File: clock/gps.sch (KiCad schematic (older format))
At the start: 12 parts, among them P301 MCRF, Q301 BSS138, U301 Adafruit746, U302 MIC5225, U303 PA6H

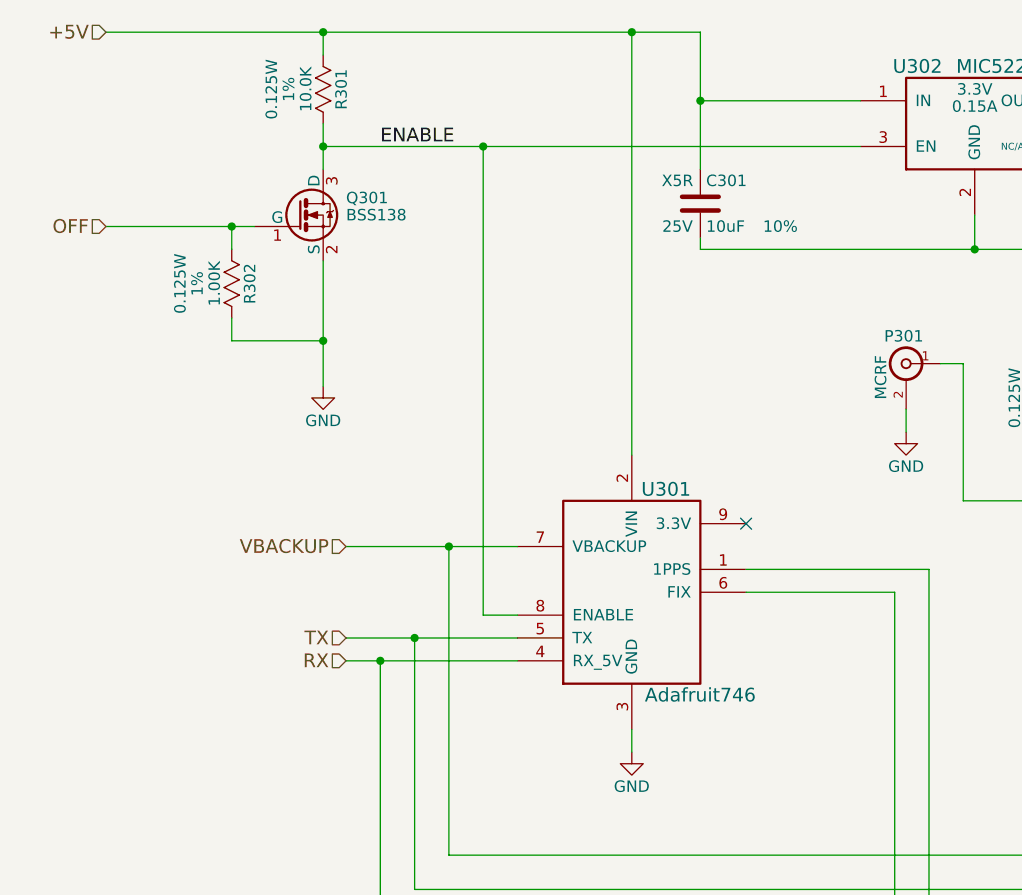
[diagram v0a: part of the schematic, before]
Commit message: Start next revision of the main board. Power sequencing and control changes.
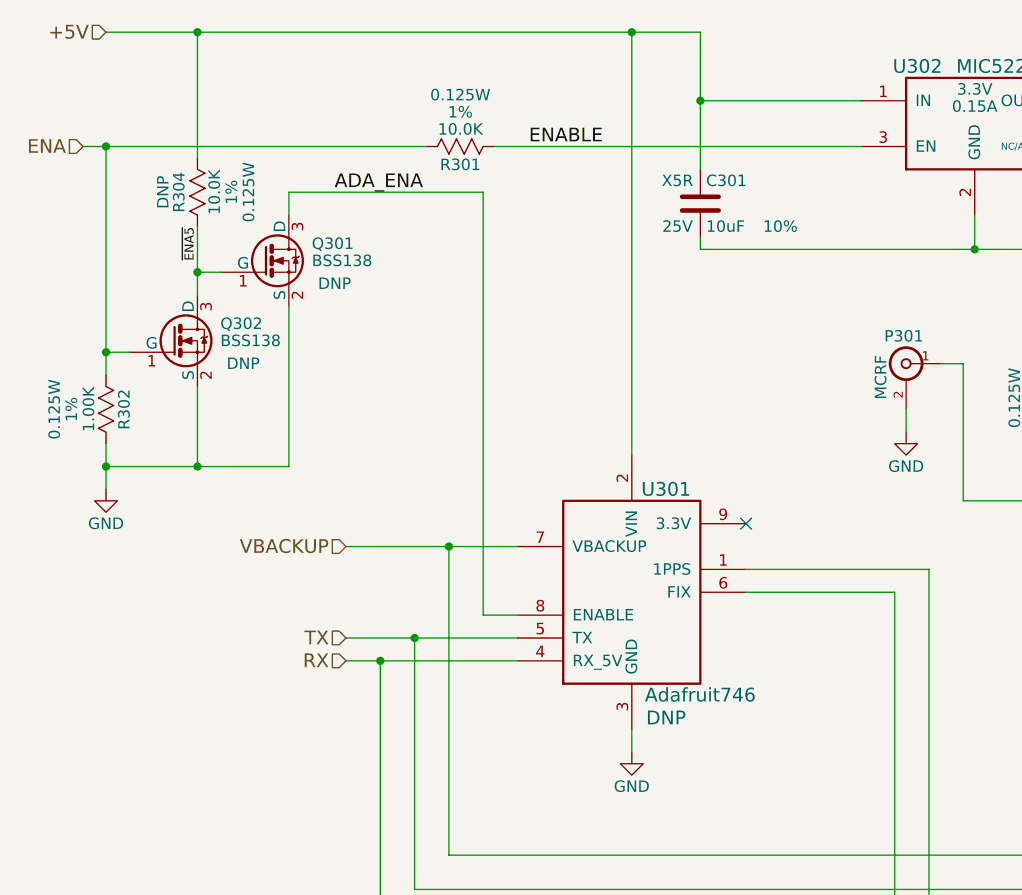
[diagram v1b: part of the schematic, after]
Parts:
- added Q302: BSS138, local:SOT-23-3_NXP_HandSoldering, symbol BSS138
- added R304: 10.0K, Resistors_SMD:R_0805_HandSoldering, symbol R_local
- Q301, U301: DNP (none) -> DNP
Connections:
- net +5V: now also R304.2; no longer R301.1
- net ENABLE: now also R301.1; no longer Q301.3 (D), R301.2, U301.8 (ENABLE)
- net GND: now also Q302.2 (S)
- net OFF renamed ENA
- net ENA: now also R301.2, Q302.1 (G); no longer Q301.1 (G)
- new net ADA_ENA: Q301.3 (D), U301.8 (ENABLE)
- new net ~ENA5~: Q301.1 (G), Q302.3 (D), R304.1
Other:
- moved on the sheet: Q301, R301, R302
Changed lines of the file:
@@
 $EndComp
 $Comp
-L GND #PWR040
+L GND #PWR041
 U 1 1 56235A8F
 P 7200 5350
-F 0 "#PWR040" H 7200 5100 50  0001 C CNN
+F 0 "#PWR041" H 7200 5100 50  0001 C CNN
 F 1 "GND" H 7200 5200 50  0000 C CNN
 F 2 "" H 7200 5350 60  0000 C CNN
@@
 Connection ~ 7100 1900
 $Comp
-L GND #PWR041
+L GND #PWR042
 U 1 1 56235D57
 P 8000 2650
-F 0 "#PWR041" H 8000 2400 50  0001 C CNN
+F 0 "#PWR042" H 8000 2400 50  0001 C CNN
 F 1 "GND" H 8000 2500 50  0000 C CNN
 F 2 "" H 8000 2650 60  0000 C CNN
@@
 Connection ~ 5250 2550
 Connection ~ 7100 2550
-Wire Wire Line
-	2400 2000 2400 2200
-Wire Wire Line
-	2400 2100 4750 2100
-Connection ~ 2400 2100
 Text HLabel 1450 1600 0    60   Input ~ 0
 +5V
-Text HLabel 1450 2450 0    60   Input ~ 0
-OFF
+Text HLabel 1350 2100 0    60   Input ~ 0
+ENA
 Text HLabel 2500 4250 0    60   Input ~ 0
 TX
@@
 	5200 3650 6300 3650
 $Comp
-L GND #PWR042
+L GND #PWR043
 U 1 1 56236310
 P 4950 3350
-F 0 "#PWR042" H 4950 3100 50  0001 C CNN
+F 0 "#PWR043" H 4950 3100 50  0001 C CNN
 F 1 "GND" H 4950 3200 50  0000 C CNN
 F 2 "" H 4950 3350 60  0000 C CNN
@@
 	2500 3850 3250 3850
 $Comp
-L GND #PWR043
+L GND #PWR044
 U 1 1 56236487
 P 3750 4750
-F 0 "#PWR043" H 3750 4500 50  0001 C CNN
+F 0 "#PWR044" H 3750 4500 50  0001 C CNN
 F 1 "GND" H 3750 4600 50  0000 C CNN
 F 2 "" H 3750 4750 60  0000 C CNN
@@
 GND
 $Comp
-L GND #PWR044
+L GND #PWR045
 U 1 1 5624967B
 P 2750 6200
-F 0 "#PWR044" H 2750 5950 50  0001 C CNN
+F 0 "#PWR045" H 2750 5950 50  0001 C CNN
 F 1 "GND" H 2750 6050 50  0000 C CNN
 F 2 "" H 2750 6200 60  0000 C CNN
@@
 F 4 "Adafruit" H 3950 3525 50  0001 C CNN "Manufacturer"
 F 5 "Adafruit746" H 4025 3450 50  0001 C CNN "PartNum"
+F 6 "DNP" H 3900 3500 60  0000 C CNN "DNP"
 	1    3750 4050
 	1    0    0    -1
@@
 L R_local R301
 U 1 1 5632AC0C
-P 2400 1850
-F 0 "R301" V 2480 1850 50  0000 C CNN
-F 1 "10.0K" V 2325 1850 50  0000 C CNN
-F 2 "Resistors_SMD:R_0805_HandSoldering" V 2330 1850 30  0001 C CNN
-F 3 "" V 2480 1850 30  0000 C CNN
-F 4 "1%" V 2250 1850 50  0000 C CNN "Tolerance"
-F 5 "0.125W" V 2175 1850 50  0000 C CNN "Power"
-F 6 "Vishay Dale" V 2400 1850 50  0001 C CNN "Manufacturer"
-F 7 "CRCW080510K0FKEA" V 2550 1850 50  0001 C CNN "PartNum"
-	1    2400 1850
-	1    0    0    -1
+P 3000 2100
+F 0 "R301" V 3080 2100 50  0000 C CNN
+F 1 "10.0K" V 2925 2100 50  0000 C CNN
+F 2 "Resistors_SMD:R_0805_HandSoldering" V 2930 2100 30  0001 C CNN
+F 3 "" V 3080 2100 30  0000 C CNN
+F 4 "1%" V 2850 2100 50  0000 C CNN "Tolerance"
+F 5 "0.125W" V 2775 2100 50  0000 C CNN "Power"
+F 6 "Vishay Dale" V 3000 2100 50  0001 C CNN "Manufacturer"
+F 7 "CRCW080510K0FKEA" V 3150 2100 50  0001 C CNN "PartNum"
+	1    3000 2100
+	0    1    1    0
 $EndComp
 NoConn ~ 5750 2100
@@
 FILT_GPS_3.3V
 $Comp
-L PWR_FLAG #FLG045
+L PWR_FLAG #FLG046
 U 1 1 5643829E
 P 7750 1800
-F 0 "#FLG045" H 7750 1895 50  0001 C CNN
+F 0 "#FLG046" H 7750 1895 50  0001 C CNN
 F 1 "PWR_FLAG" H 7750 1980 50  0000 C CNN
 F 2 "" H 7750 1800 60  0000 C CNN
@@
 L BSS138 Q301
 U 1 1 57AB6857
-P 2300 2400
-F 0 "Q301" H 2500 2475 50  0000 L CNN
-F 1 "BSS138" H 2500 2400 50  0000 L CNN
-F 2 "local:SOT-23-3_NXP_HandSoldering" H 2500 2325 50  0001 L CIN
-F 3 "" H 2300 2400 50  0000 L CNN
-F 4 "ON Semiconductor" H 2300 2400 60  0001 C CNN "Manufacturer"
-F 5 "BSS138LT1G" H 2300 2400 60  0001 C CNN "PartNum"
-	1    2300 2400
-	1    0    0    -1
-$EndComp
-Wire Wire Line
-	2400 1700 2400 1600
-Connection ~ 2400 1600
+P 2150 2600
+F 0 "Q301" H 2350 2675 50  0000 L CNN
+F 1 "BSS138" H 2350 2600 50  0000 L CNN
+F 2 "local:SOT-23-3_NXP_HandSoldering" H 2350 2525 50  0001 L CIN
+F 3 "" H 2150 2600 50  0000 L CNN
+F 4 "ON Semiconductor" H 2150 2600 60  0001 C CNN "Manufacturer"
+F 5 "BSS138LT1G" H 2150 2600 60  0001 C CNN "PartNum"
+F 6 "DNP" H 2450 2500 50  0000 C CNN "DNP"
+	1    2150 2600
+	1    0    0    -1
+$EndComp
 Connection ~ 4050 1900
-Wire Wire Line
-	1450 2450 2100 2450
-$Comp
-L GND #PWR046
+$Comp
+L GND #PWR047
 U 1 1 57AB6F8A
-P 2400 3150
-F 0 "#PWR046" H 2400 2900 50  0001 C CNN
-F 1 "GND" H 2400 3000 50  0000 C CNN
-F 2 "" H 2400 3150 60  0000 C CNN
-F 3 "" H 2400 3150 60  0000 C CNN
-	1    2400 3150
-	1    0    0    -1
-$EndComp
-Wire Wire Line
-	2400 2600 2400 3150
+P 1450 3600
+F 0 "#PWR047" H 1450 3350 50  0001 C CNN
+F 1 "GND" H 1450 3450 50  0000 C CNN
+F 2 "" H 1450 3600 60  0000 C CNN
+F 3 "" H 1450 3600 60  0000 C CNN
+	1    1450 3600
+	1    0    0    -1
+$EndComp
+Wire Wire Line
+	1450 3400 1450 3600
 $Comp
 L R_local R302
 U 1 1 57AB6FA9
-P 2000 2700
-F 0 "R302" V 2080 2700 50  0000 C CNN
-F 1 "1.00K" V 1925 2700 50  0000 C CNN
-F 2 "Resistors_SMD:R_0805_HandSoldering" V 1930 2700 30  0001 C CNN
-F 3 "" V 2080 2700 30  0000 C CNN
-F 4 "1%" V 1850 2700 50  0000 C CNN "Tolerance"
-F 5 "0.125W" V 1775 2700 50  0000 C CNN "Power"
-F 6 "Vishay Dale" V 2000 2700 50  0001 C CNN "Manufacturer"
-F 7 "CRCW080510K0FKEA" V 2150 2700 50  0001 C CNN "PartNum"
-	1    2000 2700
-	1    0    0    -1
-$EndComp
-Wire Wire Line
-	2000 2550 2000 2450
-Connection ~ 2000 2450
-Wire Wire Line
-	2000 2850 2000 2950
-Wire Wire Line
-	2000 2950 2400 2950
-Connection ~ 2400 2950
-Connection ~ 3100 2100
-Wire Wire Line
-	3250 4150 3100 4150
-Wire Wire Line
-	3100 4150 3100 2100
+P 1450 3250
+F 0 "R302" V 1530 3250 50  0000 C CNN
+F 1 "1.00K" V 1375 3250 50  0000 C CNN
+F 2 "Resistors_SMD:R_0805_HandSoldering" V 1380 3250 30  0001 C CNN
+F 3 "" V 1530 3250 30  0000 C CNN
+F 4 "1%" V 1300 3250 50  0000 C CNN "Tolerance"
+F 5 "0.125W" V 1225 3250 50  0000 C CNN "Power"
+F 6 "Vishay Dale" V 1450 3250 50  0001 C CNN "Manufacturer"
+F 7 "CRCW080510K0FKEA" V 1600 3250 50  0001 C CNN "PartNum"
+	1    1450 3250
+	1    0    0    -1
+$EndComp
+Wire Wire Line
+	3100 4150 3250 4150
+Wire Wire Line
+	3100 2300 3100 4150
 $Comp
 L R_local R303
@@
 	5650 3050 5650 2750
 Connection ~ 7000 2750
-Text Label 2650 2100 0    60   ~ 0
+Text Label 3300 2100 0    60   ~ 0
 ENABLE
+$Comp
+L BSS138 Q302
+U 1 1 57B4A861
+P 1750 2950
+F 0 "Q302" H 1950 3025 50  0000 L CNN
+F 1 "BSS138" H 1950 2950 50  0000 L CNN
+F 2 "local:SOT-23-3_NXP_HandSoldering" H 1950 2875 50  0001 L CIN
+F 3 "" H 1750 2950 50  0000 L CNN
+F 4 "ON Semiconductor" H 1750 2950 60  0001 C CNN "Manufacturer"
+F 5 "BSS138LT1G" H 1750 2950 60  0001 C CNN "PartNum"
+F 6 "DNP" H 2050 2850 50  0000 C CNN "DNP"
+	1    1750 2950
+	1    0    0    -1
+$EndComp
+Wire Wire Line
+	3150 2100 4750 2100
+$Comp
+L R_local R304
+U 1 1 57B4AD05
+P 1850 2300
+F 0 "R304" V 1930 2300 50  0000 C CNN
+F 1 "10.0K" V 1775 2300 50  0000 C CNN
+F 2 "Resistors_SMD:R_0805_HandSoldering" V 1780 2300 30  0001 C CNN
+F 3 "" V 1930 2300 30  0000 C CNN
+F 4 "1%" V 1700 2300 50  0000 C CNN "Tolerance"
+F 5 "0.125W" V 1625 2300 50  0000 C CNN "Power"
+F 6 "Vishay Dale" V 1850 2300 50  0001 C CNN "Manufacturer"
+F 7 "CRCW080510K0FKEA" V 2000 2300 50  0001 C CNN "PartNum"
+F 8 "DNP" V 2000 2300 50  0000 C CNN "DNP"
+	1    1850 2300
+	-1   0    0    1
+$EndComp
+Wire Wire Line
+	1450 2100 1450 3100
+Wire Wire Line
+	1450 3000 1550 3000
+Wire Wire Line
+	1450 3500 2250 3500
+Wire Wire Line
+	1850 3500 1850 3150
+Connection ~ 1450 3500
+Wire Wire Line
+	2250 3500 2250 2800
+Connection ~ 1850 3500
+Wire Wire Line
+	1850 2450 1850 2750
+Wire Wire Line
+	1850 2650 1950 2650
+Connection ~ 1850 2650
+Wire Wire Line
+	1850 2150 1850 1600
+Connection ~ 1850 1600
+Wire Wire Line
+	2250 2400 2250 2300
+Wire Wire Line
+	2250 2300 3100 2300
+Wire Wire Line
+	1350 2100 2850 2100
+Connection ~ 1450 3000
+Connection ~ 1450 2100
+Text Label 2450 2300 0    60   ~ 0
+ADA_ENA
+Text Label 1850 2600 1    40   ~ 0
+~ENA5~
 $EndSCHEMATC

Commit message: Checkpoint layout. Update hand soldering footprints for 0805 parts.
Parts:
- C303: footprint Capacitors_SMD:C_0805_HandSoldering -> local:C_0805_HandSoldering
- R301, R302, R303, R304: footprint Resistors_SMD:R_0805_HandSoldering -> local:R_0805_HandSoldering
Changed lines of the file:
@@
 $EndComp
 $Comp
-L GND #PWR041
+L GND #PWR040
 U 1 1 56235A8F
 P 7200 5350
-F 0 "#PWR041" H 7200 5100 50  0001 C CNN
+F 0 "#PWR040" H 7200 5100 50  0001 C CNN
 F 1 "GND" H 7200 5200 50  0000 C CNN
 F 2 "" H 7200 5350 60  0000 C CNN
@@
 Connection ~ 7100 1900
 $Comp
-L GND #PWR042
+L GND #PWR041
 U 1 1 56235D57
 P 8000 2650
-F 0 "#PWR042" H 8000 2400 50  0001 C CNN
+F 0 "#PWR041" H 8000 2400 50  0001 C CNN
 F 1 "GND" H 8000 2500 50  0000 C CNN
 F 2 "" H 8000 2650 60  0000 C CNN
@@
 	5200 3650 6300 3650
 $Comp
-L GND #PWR043
+L GND #PWR042
 U 1 1 56236310
 P 4950 3350
-F 0 "#PWR043" H 4950 3100 50  0001 C CNN
+F 0 "#PWR042" H 4950 3100 50  0001 C CNN
 F 1 "GND" H 4950 3200 50  0000 C CNN
 F 2 "" H 4950 3350 60  0000 C CNN
@@
 	2500 3850 3250 3850
 $Comp
-L GND #PWR044
+L GND #PWR043
 U 1 1 56236487
 P 3750 4750
-F 0 "#PWR044" H 3750 4500 50  0001 C CNN
+F 0 "#PWR043" H 3750 4500 50  0001 C CNN
 F 1 "GND" H 3750 4600 50  0000 C CNN
 F 2 "" H 3750 4750 60  0000 C CNN
@@
 GND
 $Comp
-L GND #PWR045
+L GND #PWR044
 U 1 1 5624967B
 P 2750 6200
-F 0 "#PWR045" H 2750 5950 50  0001 C CNN
+F 0 "#PWR044" H 2750 5950 50  0001 C CNN
 F 1 "GND" H 2750 6050 50  0000 C CNN
 F 2 "" H 2750 6200 60  0000 C CNN
@@
 F 0 "C303" H 8025 2250 50  0000 L CNN
 F 1 "0.1uF" H 8025 2050 50  0000 L CNN
-F 2 "Capacitors_SMD:C_0805_HandSoldering" H 8038 2000 30  0001 C CNN
+F 2 "local:C_0805_HandSoldering" H 8038 2000 30  0001 C CNN
 F 3 "" H 8000 2150 60  0000 C CNN
 F 4 "50V" H 7900 2050 50  0000 C CNN "Voltage"
@@
 F 0 "R301" V 3080 2100 50  0000 C CNN
 F 1 "10.0K" V 2925 2100 50  0000 C CNN
-F 2 "Resistors_SMD:R_0805_HandSoldering" V 2930 2100 30  0001 C CNN
+F 2 "local:R_0805_HandSoldering" V 2930 2100 30  0001 C CNN
 F 3 "" V 3080 2100 30  0000 C CNN
 F 4 "1%" V 2850 2100 50  0000 C CNN "Tolerance"
@@
 FILT_GPS_3.3V
 $Comp
-L PWR_FLAG #FLG046
+L PWR_FLAG #FLG045
 U 1 1 5643829E
 P 7750 1800
-F 0 "#FLG046" H 7750 1895 50  0001 C CNN
+F 0 "#FLG045" H 7750 1895 50  0001 C CNN
 F 1 "PWR_FLAG" H 7750 1980 50  0000 C CNN
 F 2 "" H 7750 1800 60  0000 C CNN
@@
 Connection ~ 4050 1900
 $Comp
-L GND #PWR047
+L GND #PWR046
 U 1 1 57AB6F8A
 P 1450 3600
-F 0 "#PWR047" H 1450 3350 50  0001 C CNN
+F 0 "#PWR046" H 1450 3350 50  0001 C CNN
 F 1 "GND" H 1450 3450 50  0000 C CNN
 F 2 "" H 1450 3600 60  0000 C CNN
@@
 F 0 "R302" V 1530 3250 50  0000 C CNN
 F 1 "1.00K" V 1375 3250 50  0000 C CNN
-F 2 "Resistors_SMD:R_0805_HandSoldering" V 1380 3250 30  0001 C CNN
+F 2 "local:R_0805_HandSoldering" V 1380 3250 30  0001 C CNN
 F 3 "" V 1530 3250 30  0000 C CNN
 F 4 "1%" V 1300 3250 50  0000 C CNN "Tolerance"
@@
 F 0 "R303" V 5730 3200 50  0000 C CNN
 F 1 "10.0K" V 5575 3200 50  0000 C CNN
-F 2 "Resistors_SMD:R_0805_HandSoldering" V 5580 3200 30  0001 C CNN
+F 2 "local:R_0805_HandSoldering" V 5580 3200 30  0001 C CNN
 F 3 "" V 5730 3200 30  0000 C CNN
 F 4 "1%" V 5500 3200 50  0000 C CNN "Tolerance"
@@
 F 0 "R304" V 1930 2300 50  0000 C CNN
 F 1 "10.0K" V 1775 2300 50  0000 C CNN
-F 2 "Resistors_SMD:R_0805_HandSoldering" V 1780 2300 30  0001 C CNN
+F 2 "local:R_0805_HandSoldering" V 1780 2300 30  0001 C CNN
 F 3 "" V 1930 2300 30  0000 C CNN
 F 4 "1%" V 1700 2300 50  0000 C CNN "Tolerance"

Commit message: Checkpoint layout. Change SOT-23-5 to hand soldering version.
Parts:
- U302: footprint local:SOT-23-5_1.6x2.9mm_Pitch0.95mm -> local:SOT-23-5_1.6x2.9mm_Pitch0.95mm_HandSoldering
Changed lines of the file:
@@
 F 0 "U302" H 5000 2250 60  0000 C CNN
 F 1 "MIC5225" H 5350 2250 60  0000 C CNN
-F 2 "local:SOT-23-5_1.6x2.9mm_Pitch0.95mm" H 5050 2000 60  0001 C CNN
+F 2 "local:SOT-23-5_1.6x2.9mm_Pitch0.95mm_HandSoldering" H 5050 2000 60  0001 C CNN
 F 3 "" H 5050 2000 60  0000 C CNN
 F 4 "3.3V" H 5250 2150 50  0000 C CNN "Voltage"

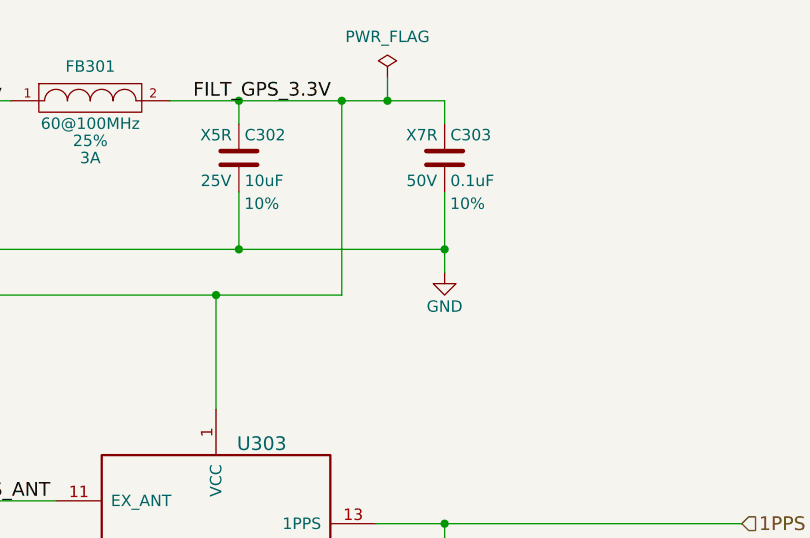
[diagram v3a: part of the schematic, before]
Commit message: Add power indication LEDs.
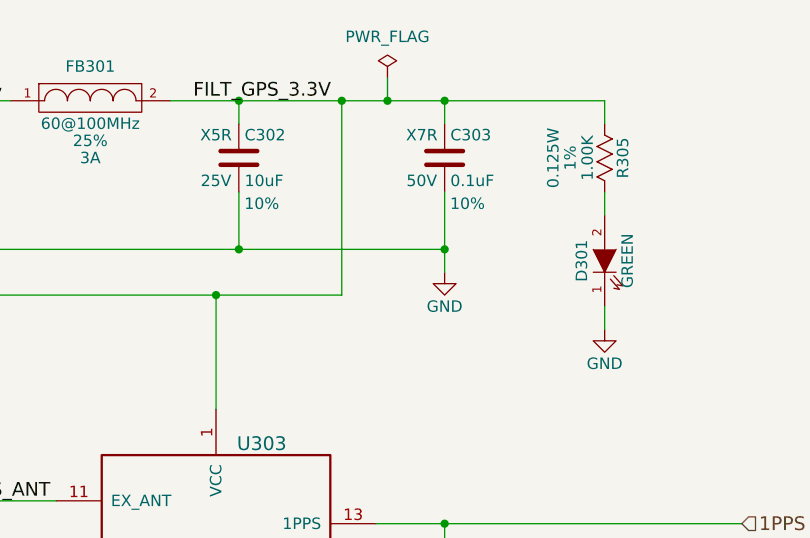
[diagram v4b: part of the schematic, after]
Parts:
- added D301: GREEN, local:LED_0805_HandSoldering, symbol LED
- added R305: 1.00K, local:R_0805_HandSoldering, symbol R_local
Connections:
- net FILT_GPS_3.3V: now also R305.1
- net GND: now also D301.1 (K)
- new net: D301.2 (A), R305.2
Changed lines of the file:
@@
 $EndComp
 $Comp
-L GND #PWR040
+L GND #PWR305
 U 1 1 56235A8F
 P 7200 5350
-F 0 "#PWR040" H 7200 5100 50  0001 C CNN
+F 0 "#PWR305" H 7200 5100 50  0001 C CNN
 F 1 "GND" H 7200 5200 50  0000 C CNN
 F 2 "" H 7200 5350 60  0000 C CNN
@@
 	5750 1900 6100 1900
 Wire Wire Line
-	6800 1900 8000 1900
+	6800 1900 8700 1900
 Wire Wire Line
 	7100 2000 7100 1900
 Connection ~ 7100 1900
 $Comp
-L GND #PWR041
+L GND #PWR306
 U 1 1 56235D57
 P 8000 2650
-F 0 "#PWR041" H 8000 2400 50  0001 C CNN
+F 0 "#PWR306" H 8000 2400 50  0001 C CNN
 F 1 "GND" H 8000 2500 50  0000 C CNN
 F 2 "" H 8000 2650 60  0000 C CNN
@@
 	5200 3650 6300 3650
 $Comp
-L GND #PWR042
+L GND #PWR304
 U 1 1 56236310
 P 4950 3350
-F 0 "#PWR042" H 4950 3100 50  0001 C CNN
+F 0 "#PWR304" H 4950 3100 50  0001 C CNN
 F 1 "GND" H 4950 3200 50  0000 C CNN
 F 2 "" H 4950 3350 60  0000 C CNN
@@
 	2500 3850 3250 3850
 $Comp
-L GND #PWR043
+L GND #PWR303
 U 1 1 56236487
 P 3750 4750
-F 0 "#PWR043" H 3750 4500 50  0001 C CNN
+F 0 "#PWR303" H 3750 4500 50  0001 C CNN
 F 1 "GND" H 3750 4600 50  0000 C CNN
 F 2 "" H 3750 4750 60  0000 C CNN
@@
 GND
 $Comp
-L GND #PWR044
+L GND #PWR302
 U 1 1 5624967B
 P 2750 6200
-F 0 "#PWR044" H 2750 5950 50  0001 C CNN
+F 0 "#PWR302" H 2750 5950 50  0001 C CNN
 F 1 "GND" H 2750 6050 50  0000 C CNN
 F 2 "" H 2750 6200 60  0000 C CNN
@@
 FILT_GPS_3.3V
 $Comp
-L PWR_FLAG #FLG045
+L PWR_FLAG #FLG301
 U 1 1 5643829E
 P 7750 1800
-F 0 "#FLG045" H 7750 1895 50  0001 C CNN
+F 0 "#FLG301" H 7750 1895 50  0001 C CNN
 F 1 "PWR_FLAG" H 7750 1980 50  0000 C CNN
 F 2 "" H 7750 1800 60  0000 C CNN
@@
 Connection ~ 4050 1900
 $Comp
-L GND #PWR046
+L GND #PWR301
 U 1 1 57AB6F8A
 P 1450 3600
-F 0 "#PWR046" H 1450 3350 50  0001 C CNN
+F 0 "#PWR301" H 1450 3350 50  0001 C CNN
 F 1 "GND" H 1450 3450 50  0000 C CNN
 F 2 "" H 1450 3600 60  0000 C CNN
@@
 Text Label 1850 2600 1    40   ~ 0
 ~ENA5~
+$Comp
+L R_local R305
+U 1 1 5897F099
+P 8700 2150
+F 0 "R305" V 8780 2150 50  0000 C CNN
+F 1 "1.00K" V 8625 2150 50  0000 C CNN
+F 2 "local:R_0805_HandSoldering" V 8630 2150 30  0001 C CNN
+F 3 "" V 8780 2150 30  0000 C CNN
+F 4 "1%" V 8550 2150 50  0000 C CNN "Tolerance"
+F 5 "0.125W" V 8475 2150 50  0000 C CNN "Power"
+F 6 "Vishay Dale" V 8700 2150 50  0001 C CNN "Manufacturer"
+F 7 "CRCW08051K00FKEA" V 8850 2150 50  0001 C CNN "PartNum"
+	1    8700 2150
+	1    0    0    -1
+$EndComp
+$Comp
+L LED D301
+U 1 1 5897F149
+P 8700 2600
+F 0 "D301" H 8700 2700 50  0000 C CNN
+F 1 "GREEN" H 8700 2500 50  0000 C CNN
+F 2 "local:LED_0805_HandSoldering" H 8700 2600 50  0001 C CNN
+F 3 "" H 8700 2600 50  0000 C CNN
+F 4 "Lite-On" H 8700 2600 50  0001 C CNN "Manufacturer"
+F 5 "LIST-C171GKT" H 8700 2600 50  0001 C CNN "PartNum"
+	1    8700 2600
+	0    -1   -1   0
+$EndComp
+Wire Wire Line
+	8700 2300 8700 2400
+$Comp
+L GND #PWR307
+U 1 1 5897F426
+P 8700 2900
+F 0 "#PWR307" H 8700 2650 50  0001 C CNN
+F 1 "GND" H 8700 2750 50  0000 C CNN
+F 2 "" H 8700 2900 60  0000 C CNN
+F 3 "" H 8700 2900 60  0000 C CNN
+	1    8700 2900
+	1    0    0    -1
+$EndComp
+Wire Wire Line
+	8700 2800 8700 2900
+Wire Wire Line
+	8700 1900 8700 2000
+Connection ~ 8000 1900
 $EndSCHEMATC
